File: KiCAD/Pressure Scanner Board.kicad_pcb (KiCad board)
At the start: 2 copper layers, 90 x 85 mm, 66 parts, among them J1 Cortex_Debug, J2 USB_Micro_B, J3 Battery Headers, J4 Can Header, Q1 3.7A, 30V, Q2 BSS138, Q3 BSS138, SW1 FSMCTTR, U1 SAMD21G18A-AU, U10 DLHR-L10D-E1BD-C-NAV8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

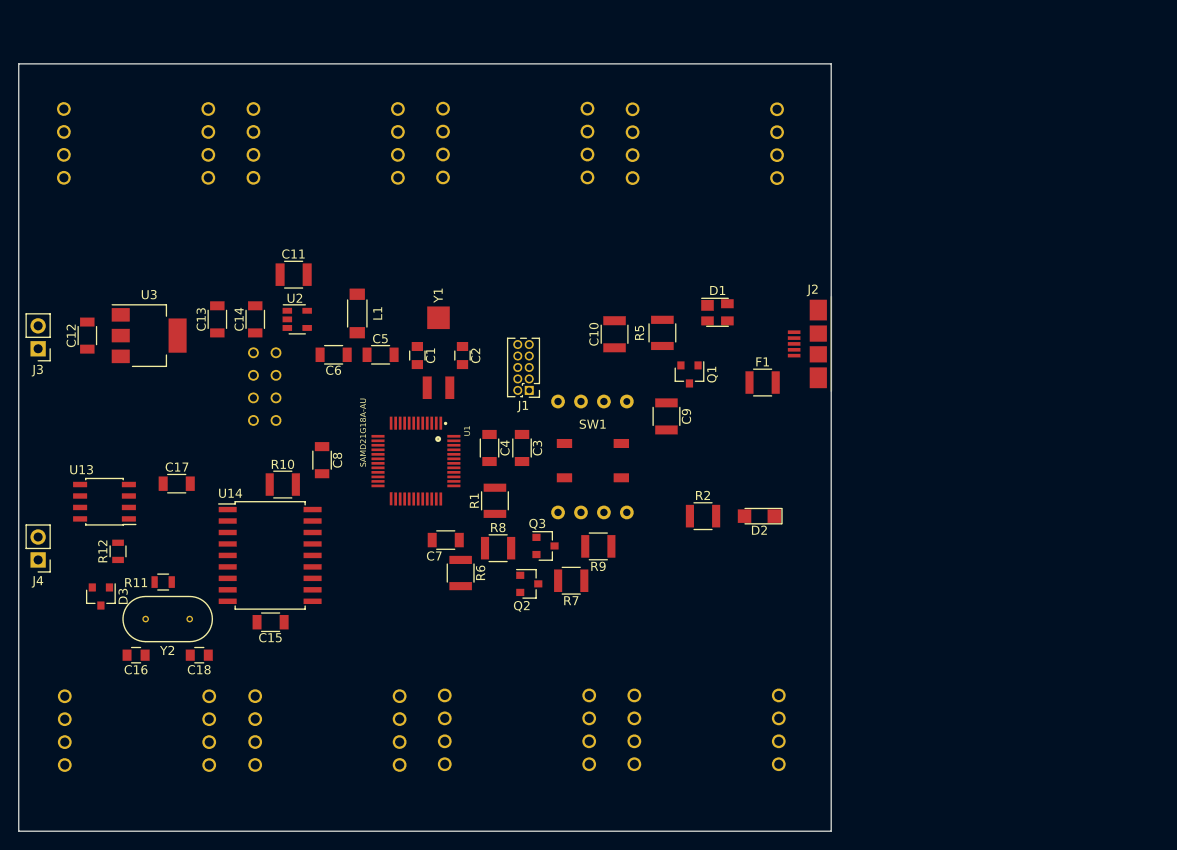
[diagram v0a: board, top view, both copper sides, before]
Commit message: Dropped 4 spare sensors, revising layout.
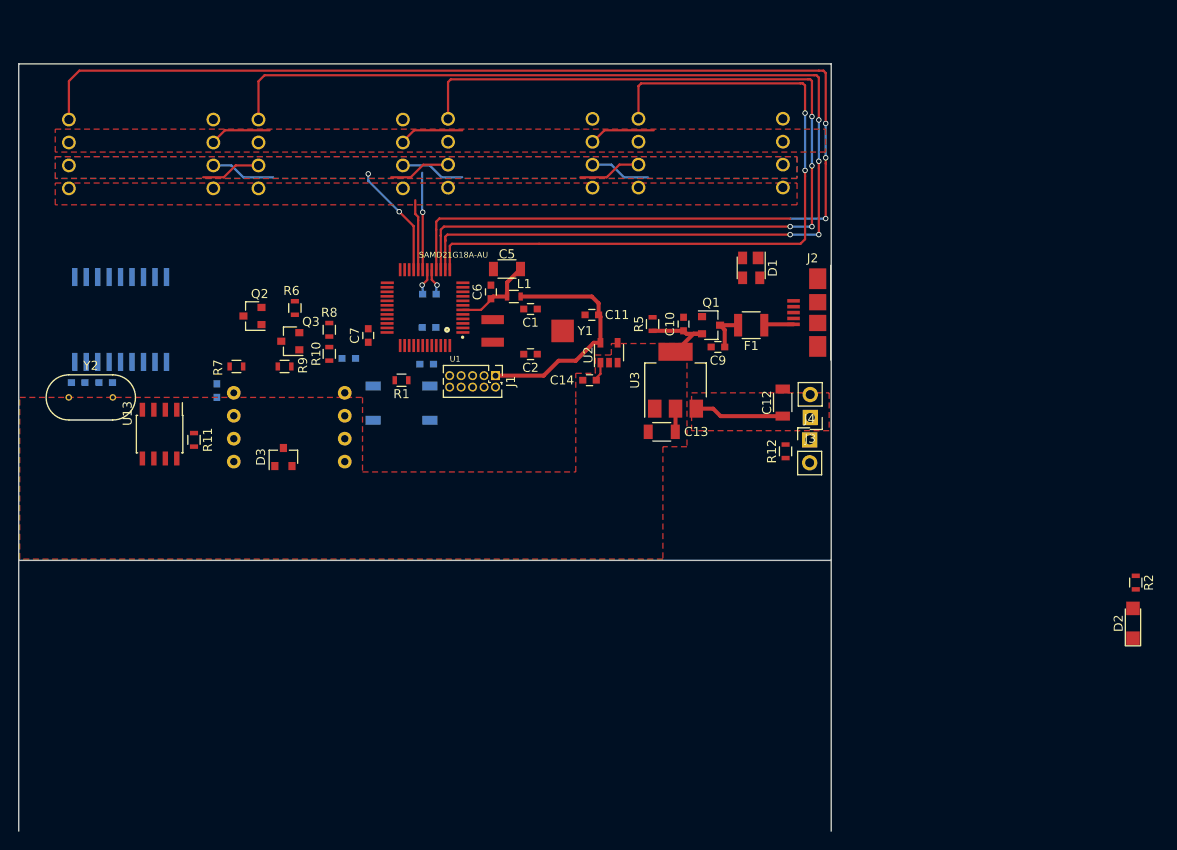
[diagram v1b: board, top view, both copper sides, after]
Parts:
- removed  : Via, Via (x9)
- removed U10, U12, U6, U8: DLHR-L10D-E1BD-C-NAV8, DLHR-L10D-E1BD-C-NAV8:DLHR-L10D-E1BD-C-NAV8
- C1, C2: footprint Capacitors_SMD:C_0805 -> Capacitors_SMD:C_0603
- C10, C11, C9: footprint Capacitors_SMD:C_1210 -> Capacitors_SMD:C_0603
- C14, C6, C7: footprint Capacitors_SMD:C_1206 -> Capacitors_SMD:C_0603
- C15, C17, C3, C4, C8: footprint Capacitors_SMD:C_1206 -> Capacitors_SMD:C_0603; moved to B.Cu
- C16, C18: footprint Capacitors_SMD:C_0805 -> Capacitors_SMD:C_0603; moved to B.Cu
- L1: footprint Inductors_SMD:L_1806 -> Inductors_SMD:L_0603
- R1, R10, R2, R5, R6, R7, R8, R9: footprint Resistors_SMD:R_1210 -> Resistors_SMD:R_0603
- R11, R12: footprint Resistors_SMD:R_0805 -> Resistors_SMD:R_0603
- SW1, U14: moved to B.Cu
- moved U5 90.2 mm to (186.7, 64.9), turned to 180 degrees
- moved U11 89.4 mm to (123.6, 65.0), turned to 180 degrees
- moved J4 86.5 mm to (197.6, 96.6), turned to 0 degrees
- moved J3 85.9 mm to (197.7, 94.2)
- moved C12 77.4 mm to (194.6, 92.5)
- moved R12 74.8 mm to (194.9, 97.9), turned to 270 degrees
- moved U9 67.4 mm to (165.6, 64.9), turned to 180 degrees
- moved U7 67.0 mm to (144.6, 65.0), turned to 180 degrees
- moved U3 58.5 mm to (182.8, 90.0), turned to 90 degrees
- moved C13 50.8 mm to (181.2, 95.8), turned to 180 degrees
- moved R2 48.5 mm to (233.7, 112.5), turned to 270 degrees
- moved R7 44.0 mm to (134.1, 88.5), turned to 0 degrees
- moved D2 43.0 mm to (233.4, 117.0), turned to 90 degrees
- moved Q2 42.7 mm to (135.9, 82.9), turned to 180 degrees
- moved R9 40.1 mm to (139.4, 88.5)
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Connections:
- J1 pad 6: Net-(J1-Pad6) -> (no net)
- J1 pad 7: Net-(J1-Pad7) -> (no net)
- J1 pad 8: Net-(J1-Pad8) -> (no net)
- J1 pad 9: Net-(J1-Pad9) -> (no net)
- J2 pad 4: Net-(J2-Pad4) -> (no net)
- U1 pad 10: SS_3 -> (no net)
- U1 pad 11: SS_4 -> (no net)
- U1 pad 12: SS_5 -> (no net)
- U1 pad 13: MISO_1 -> SS_0
- U1 pad 14: SS_6 -> SS_1
- U1 pad 15: MOSI_1 -> SS_2
- U1 pad 16: SCLK_1 -> SS_3
- U1 pad 22: SS_7 -> (no net)
- U1 pad 23: Net-(U1-Pad23) -> (no net)
- U1 pad 24: Net-(U1-Pad24) -> (no net)
- U1 pad 29: Net-(U1-Pad29) -> (no net)
- U1 pad 3: Net-(U1-Pad3) -> (no net)
- U1 pad 30: Net-(U1-Pad30) -> (no net)
- U1 pad 37: Net-(U1-Pad37) -> (no net)
- U1 pad 38: Net-(U1-Pad38) -> (no net)
- U1 pad 39: Net-(U1-Pad39) -> (no net)
- U1 pad 4: Net-(U1-Pad4) -> (no net)
- U1 pad 41: Net-(U1-Pad41) -> (no net)
- U1 pad 47: Net-(U1-Pad47) -> (no net)
- U1 pad 48: Net-(U1-Pad48) -> (no net)
- U1 pad 7: SS_0 -> (no net)
- U1 pad 8: SS_1 -> (no net)
- U1 pad 9: SS_2 -> (no net)
- U11 pad 5: Net-(U11-Pad5) -> (no net)
- U11 pad 7: Net-(U11-Pad7) -> (no net)
- U13 pad 5: Net-(U13-Pad5) -> (no net)
- U14 pad 10: Net-(U14-Pad10) -> (no net)
- U14 pad 11: Net-(U14-Pad11) -> (no net)
- U14 pad 12: CAN_INT -> (no net)
- U14 pad 3: Net-(U14-Pad3) -> (no net)
- U14 pad 4: Net-(U14-Pad4) -> (no net)
- U14 pad 5: Net-(U14-Pad5) -> (no net)
- U14 pad 6: Net-(U14-Pad6) -> (no net)
- U2 pad 4: Net-(U2-Pad4) -> (no net)
- U5 pad 5: Net-(U5-Pad5) -> (no net)
- U5 pad 7: Net-(U5-Pad7) -> (no net)
- U7 pad 5: Net-(U7-Pad5) -> (no net)
- U7 pad 7: Net-(U7-Pad7) -> (no net)
- U9 pad 5: Net-(U9-Pad5) -> (no net)
- U9 pad 7: Net-(U9-Pad7) -> (no net)
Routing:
- net SS_3: track 0.00 -> 153.4 mm, vias 0 -> 3
- net SS_1: track 0.00 -> 129.3 mm, vias 0 -> 4
- net SS_2: track 0.00 -> 106.4 mm, vias 0 -> 4
- net SS_0: track 0.00 -> 81.6 mm, vias 0 -> 2
- net +3V3: track 0.00 -> 50.9 mm, vias 0 -> 1
- net MISO_0: track 0.00 -> 33.3 mm, vias 0 -> 2
- net MOSI_0: track 0.00 -> 31.8 mm, vias 0 -> 1
- net +5V: track 0.00 -> 14.1 mm
- net +BATT: track 0.00 -> 9.92 mm
- net Net-(C5-Pad1): track 0.00 -> 9.25 mm
- net SCLK_0: track 0.00 -> 7.83 mm
- net Net-(C9-Pad1): track 0.00 -> 4.62 mm
- net VBUS: track 0.00 -> 3.28 mm
- net GND: track 0.00 -> 2.96 mm, vias 0 -> 1
- added copper zone on F.Cu, net +3V3
- added copper zone on F.Cu, net +5V
- added copper zone on F.Cu, net +BATT
- added copper zone on F.Cu, net MISO_0
- added copper zone on B.Cu, net MOSI_0
- added copper zone on F.Cu, net SCLK_0
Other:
- outline, holes or cut-outs redrawn

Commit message: Finished layout V0.01
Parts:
- removed J4: Can Header, Pin_Headers:Pin_Header_Straight_1x02_Pitch2.54mm
- added REF**: NPT-2mm, NPT-2mm, F.Cu at (113.3, 102.0)
- added REF**: NPT-2mm, NPT-2mm, F.Cu at (113.7, 52.5)
- added REF**: NPT-2mm, NPT-2mm, F.Cu at (198.1, 52.6)
- added REF**: NPT-2mm, NPT-2mm, F.Cu at (197.5, 102.2)
- C11: moved to B.Cu
- C3: moved to F.Cu
- J3: value Battery Headers -> Conn_01x04; footprint Pin_Headers:Pin_Header_Straight_1x02_Pitch2.54mm -> Pin_Headers:Pin_Header_Straight_1x04_Pitch2.54mm
- moved R2 66.1 mm to (169.9, 95.2), turned to 0 degrees
- moved D2 63.7 mm to (173.0, 96.9)
- moved C15 21.5 mm to (127.8, 77.2), turned to 90 degrees
- moved R10 19.4 mm to (127.8, 77.1)
- moved R9 5.73 mm to (133.7, 88.1), turned to 0 degrees
- moved R8 5.48 mm to (140.5, 88.3)
- moved R7 4.33 mm to (133.7, 84.2)
- moved C12 3.93 mm to (193.7, 88.7)
- moved J3 3.81 mm to (197.7, 90.4), turned to 0 degrees
- moved Q3 3.41 mm to (137.7, 88.1)
- moved C3 2.29 mm to (153.5, 89.8)
- moved Q2 2.11 mm to (137.7, 84.1)
- moved R1 2.05 mm to (151.7, 88.1)
- moved R6 2.04 mm to (140.5, 84.1)
- moved SW1 1.94 mm to (152.5, 94.5), turned to 270 degrees
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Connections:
- D3 pad 1: /CAN Bus/+ -> CAN+
- D3 pad 2: /CAN Bus/- -> CAN-
- R12 pad 1: /CAN Bus/+ -> CAN+
- R12 pad 2: /CAN Bus/- -> CAN-
- U13 pad 6: /CAN Bus/- -> CAN-
- U13 pad 7: /CAN Bus/+ -> CAN+
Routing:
- net CAN-: track 0.00 -> 85.7 mm, vias 0 -> 2
- net CAN+: track 0.00 -> 82.2 mm
- net GND: track 2.96 -> 70.0 mm, vias 1 -> 26
- net USB_D-: track 0.00 -> 55.4 mm, vias 0 -> 4
- net USB_D+: track 0.00 -> 52.0 mm, vias 0 -> 2
- net SCLK_CAN: track 0.00 -> 35.4 mm, vias 0 -> 3
- net MISO_CAN: track 0.00 -> 34.7 mm, vias 0 -> 3
- net MOSI_CAN: track 0.00 -> 34.4 mm, vias 0 -> 3
- net SS_CAN: track 0.00 -> 33.2 mm, vias 0 -> 3
- net RESETN: track 0.00 -> 22.7 mm, vias 0 -> 1
- net SDA_H: track 0.00 -> 22.3 mm, vias 0 -> 2
- net SCL_H: track 0.00 -> 20.9 mm
- net SCL_L: track 0.00 -> 16.8 mm, vias 0 -> 4
- net SWCLK: track 0.00 -> 16.2 mm
- net SWDIO: track 0.00 -> 15.5 mm, vias 0 -> 2
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- added copper zone on B.Cu, net GND
- added copper zone on F.Cu, net GND
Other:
- board size 90 x 85 mm -> 90 x 55 mm
- rule trace_min: 0.2 -> 0.19
- board text added: "To-Do: 1. Check size of static pressure sensor 2. Balance SS vias for flood placement"
- board text removed: "To-Do: 1. Mark differential pairs in eeschema for routing 2. Check size of static pressure sensor"

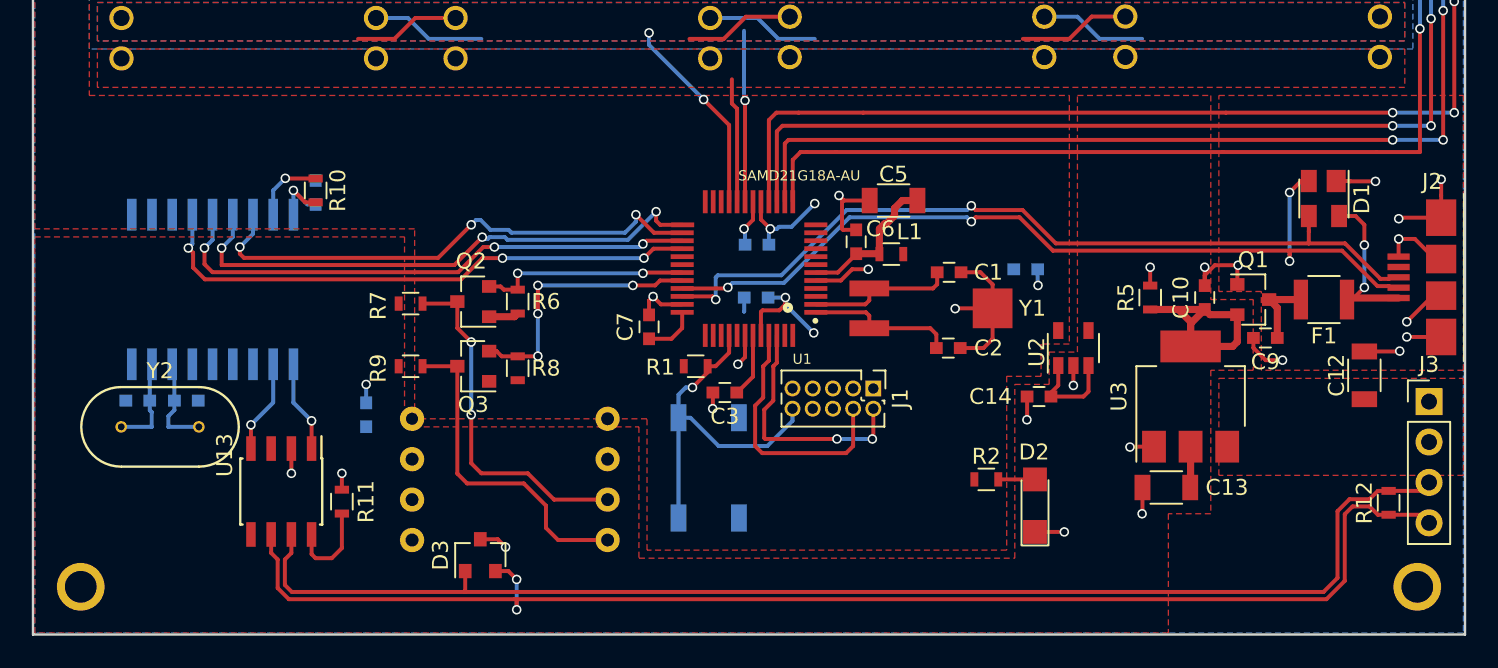
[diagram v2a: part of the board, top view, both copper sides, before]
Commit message: Tidy up soldermask, cleaned up copper pours. Waiting for final packaging design
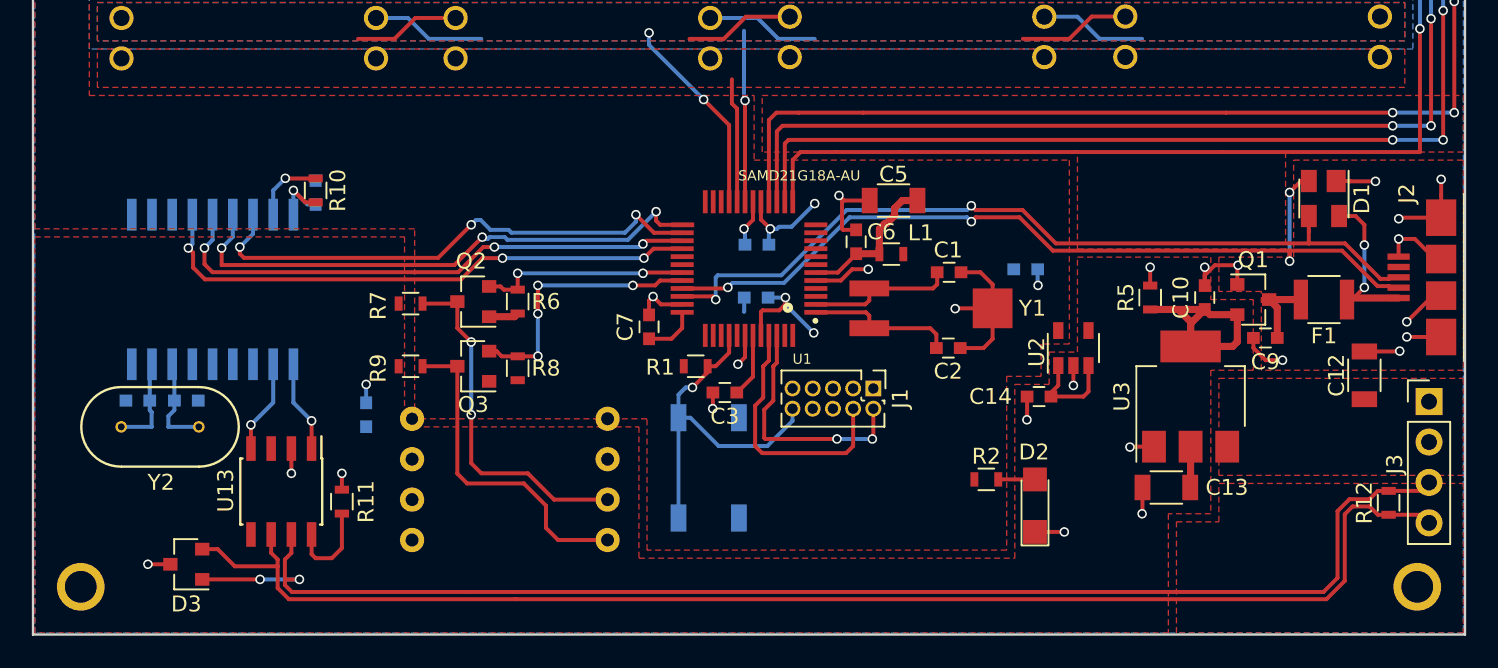
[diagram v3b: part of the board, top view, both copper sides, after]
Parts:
- moved D3 18.5 mm to (119.6, 100.6), turned to 180 degrees
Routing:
- net CAN+: track 82.2 -> 87.8 mm, vias 0 -> 2
- net CAN-: track 85.7 -> 86.7 mm, vias 2 -> 0
- added copper zone on F.Cu, net (none)
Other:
- board text added: "UConn Formula SAE Pressure Scanner Rev- Designed By M.Cox 2019"

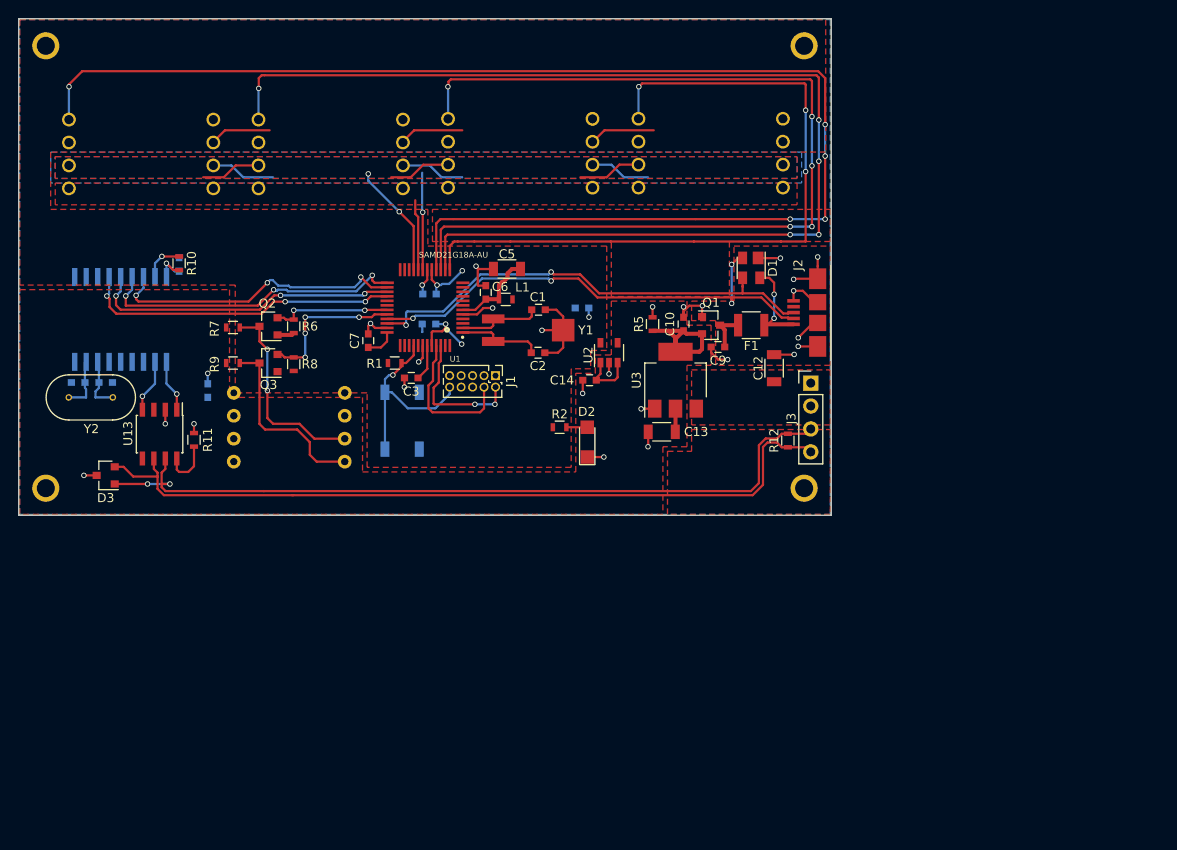
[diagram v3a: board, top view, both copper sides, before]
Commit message: Change NPTH Mounting holes and swap to JST PH Series Connector
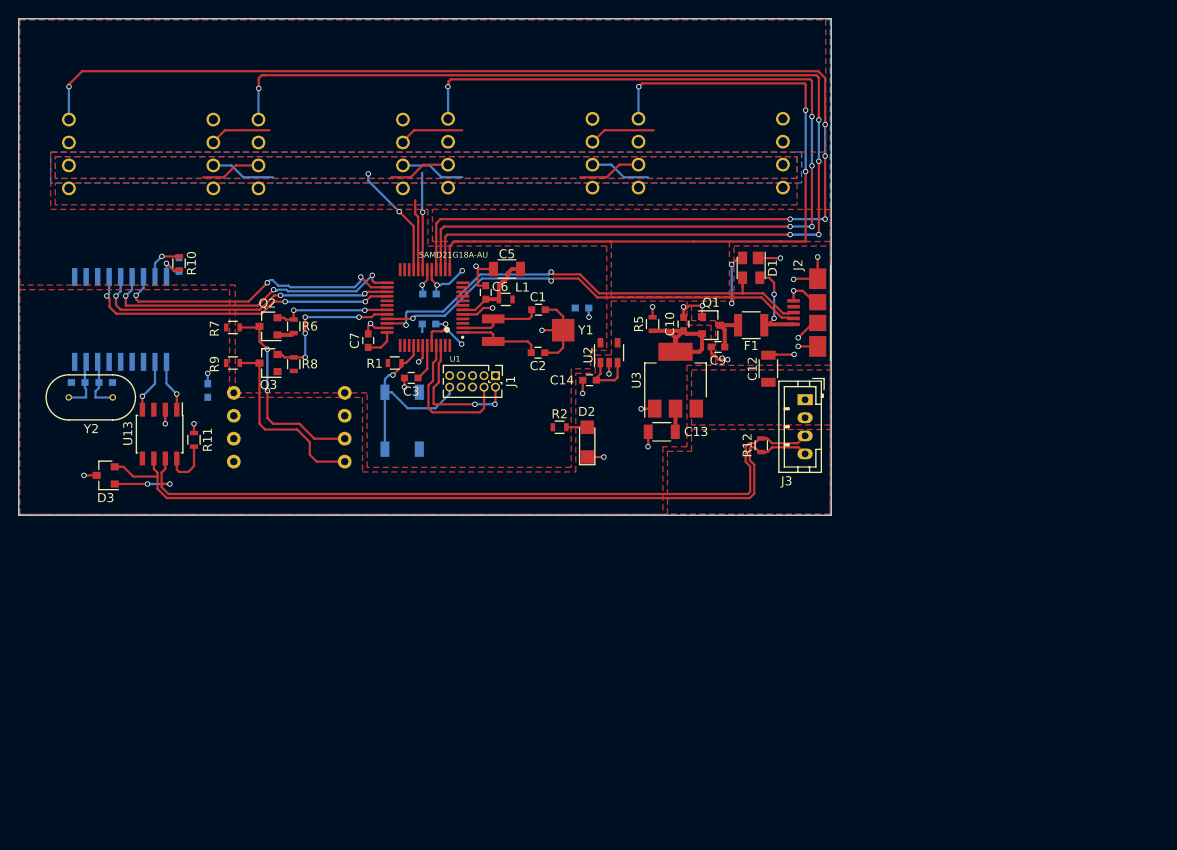
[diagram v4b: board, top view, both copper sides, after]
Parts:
- removed REF** (x4): NPT-2mm, NPT-2mm
- J3: footprint Pin_Headers:Pin_Header_Straight_1x04_Pitch2.54mm -> Connectors_JST:JST_PH_B4B-PH-K_04x2.00mm_Straight
- moved R12 3.00 mm to (192.2, 97.2)
- moved J3 1.95 mm to (197.1, 92.2), turned to 270 degrees
- moved C12 0.64 mm to (193.0, 88.8)
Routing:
- net CAN+: track 87.8 -> 88.7 mm
- net GND: track 69.6 -> 70.5 mm
- net CAN-: track 86.7 -> 87.6 mm
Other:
- rule trace_min: 0.19 -> 0.2
- board text removed: "To-Do: 1. Check size of static pressure sensor 2. Balance SS vias for flood placement"
